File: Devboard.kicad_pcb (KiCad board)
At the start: 2 copper layers, 27.6 x 23 mm, 14 parts, among them IC1 ATTINY85-P, P1 CONN_01X04, P2 CONN_01X04, P3 CONN_01X03, P4 CONN_02X03, U1 AMS1117-5.0

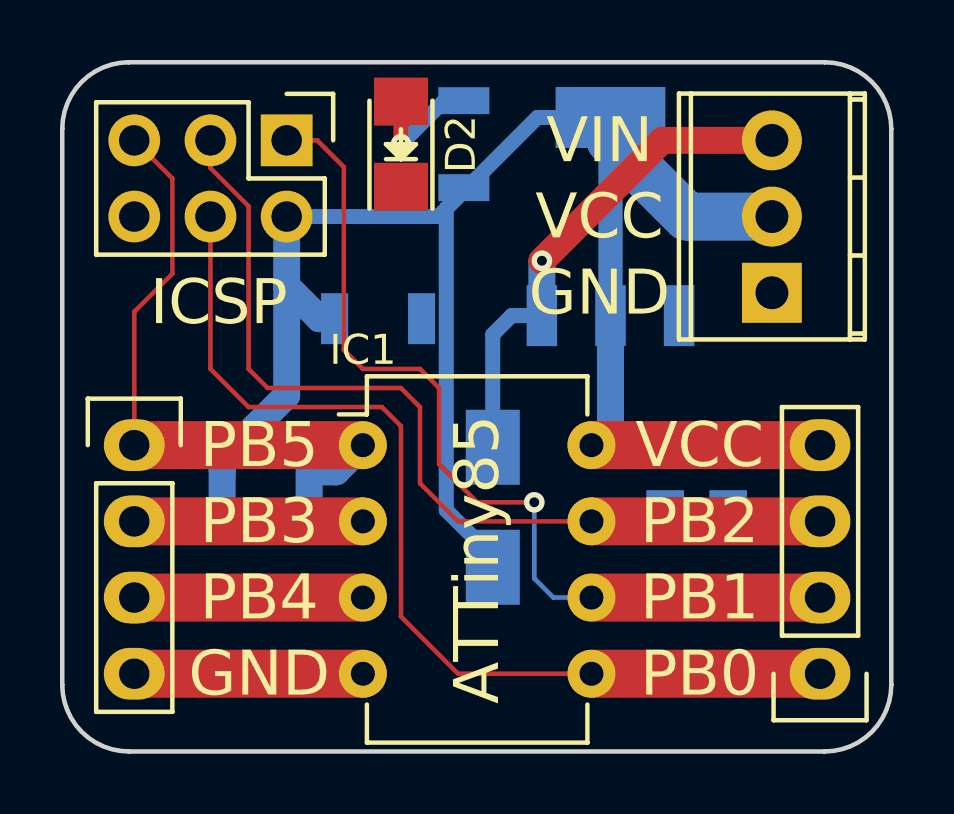
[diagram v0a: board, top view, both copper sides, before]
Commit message: Final version
Board I ended up ordering from OSH Park.
It's small, so the pricing is good enough.
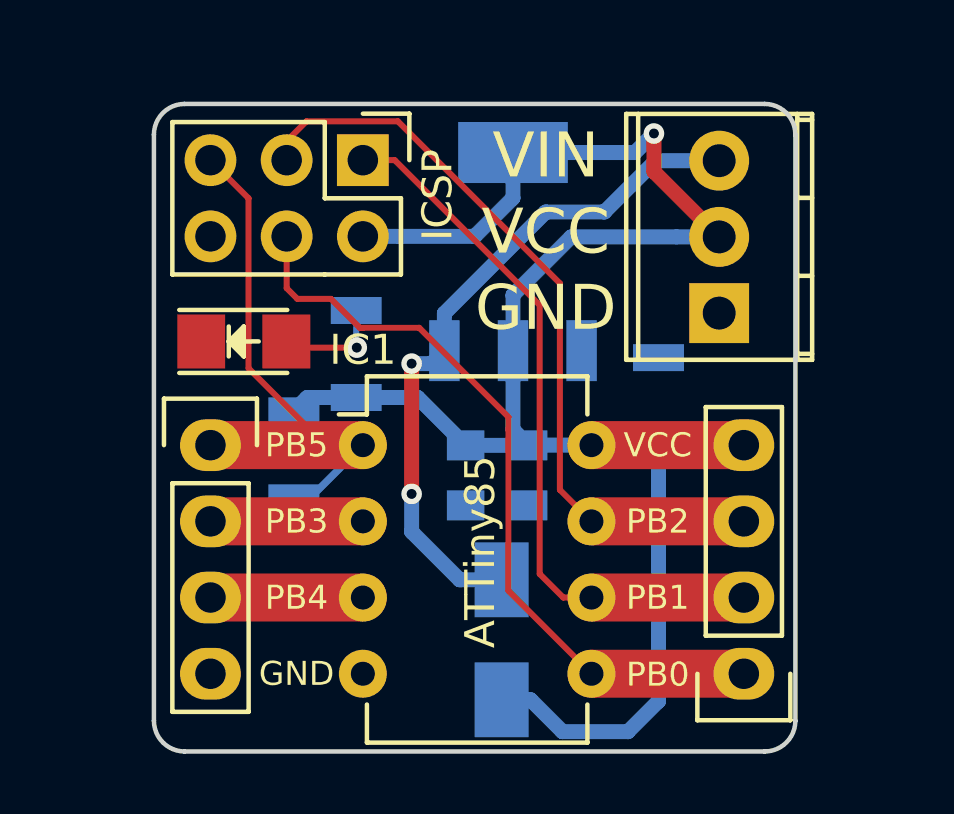
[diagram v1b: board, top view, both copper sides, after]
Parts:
- removed REF**: Symbol_OSHW-Logo_SilkScreen, Symbols:Symbol_OSHW-Logo_SilkScreen
- moved R1 9.74 mm to (182.6, 107.8), turned to 90 degrees
- moved D2 8.41 mm to (168.7, 105.8), turned to 0 degrees
- moved R3 7.86 mm to (172.5, 106.2)
- moved C2 6.65 mm to (176.1, 110.2)
- moved C1 6.65 mm to (178.2, 110.2)
- moved D1 4.43 mm to (177.3, 115.7)
- moved U1 3.45 mm to (177.7, 102.8)
- moved P4 2.62 mm to (172.7, 99.7)
- moved P2 2.54 mm to (185.4, 116.8)
- moved P1 2.54 mm to (167.6, 109.2)
- moved P3 1.88 mm to (184.6, 104.8)
- moved R2 1.11 mm to (170.4, 109.5), turned to 270 degrees
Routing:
- net VCC: track 70.8 -> 62.4 mm, vias 0 -> 1
- net PB0: track 33.3 -> 25.7 mm
- net GND: track 7.62 -> 0.00 mm
- net PB1: track 30.6 -> 24.0 mm, vias 1 -> 0
- net +9V: track 16.8 -> 23.1 mm, vias 1 -> 2
- net PB2: track 30.8 -> 25.7 mm
- net PB4: track 7.62 -> 5.08 mm
- net PB3: track 7.62 -> 5.08 mm
- net PB5: track 21.0 -> 20.4 mm
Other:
- board size 27.6 x 23 mm -> 21.4 x 21.6 mm
- rule pad_to_mask_clearance: 0.127 -> 0.13
- rule solder_mask_min_width: 0.127 -> 0.2
- board text added: "Niko Montonen"
- board text added: "nikomo"
- board text removed: "2016 rev 1"
- board text removed: "Niko 'nikomo' Montonen"
- board text removed: "Tiny85 A tiny dev board"
